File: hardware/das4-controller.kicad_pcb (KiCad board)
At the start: 4 copper layers, 51.1 x 94 mm, 78 parts, among them J1 USB-C, J2 USB-A 1, J3 USB-A 2, J4 Key matrix, Q1 2N7002, SW1 Button 1, SW2 Button 2, SW3 Button 3, SW4 Button 4, SW5 Button 5, SW6 BOOTSEL, SW7 RESET, U1 RP2350B, U2 CH334R, U3 W25Q128JVS, U4 ME6211C33M5G-N, Y1 12MHz, Y2 12MHz

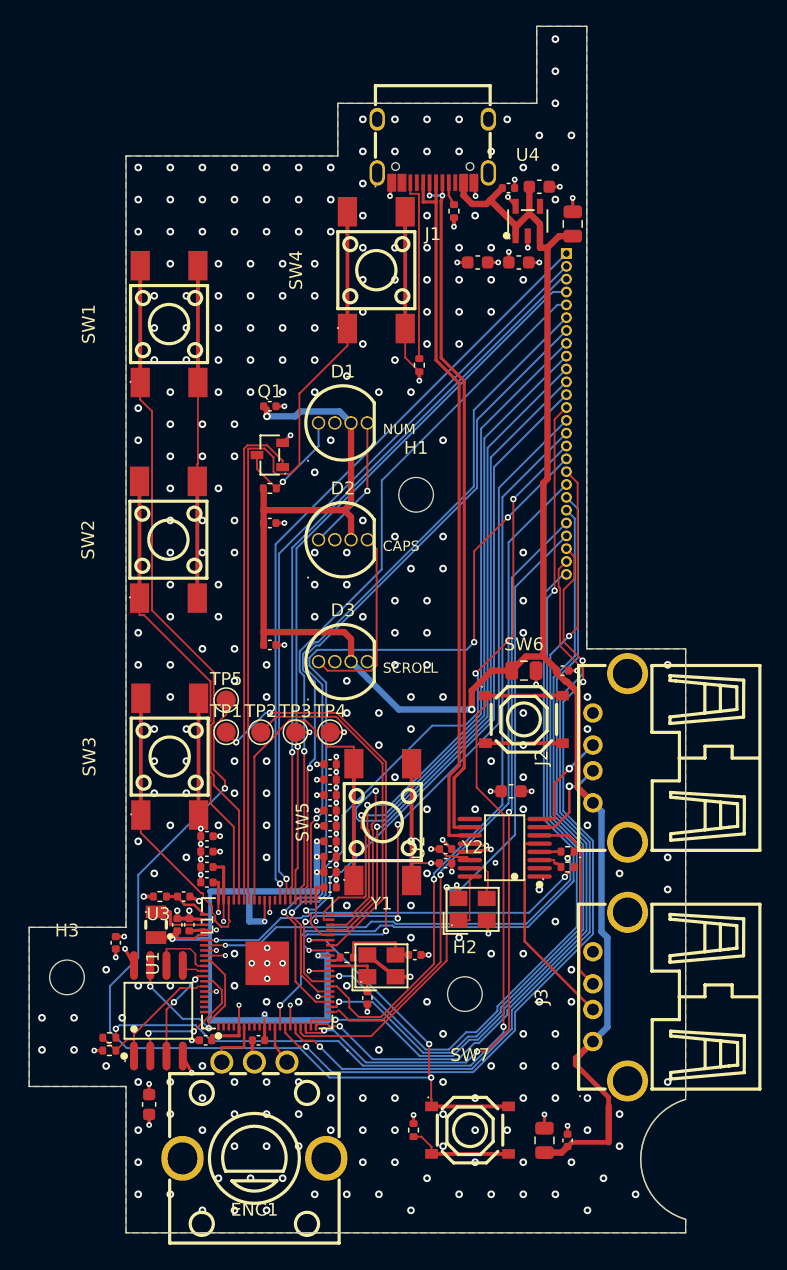
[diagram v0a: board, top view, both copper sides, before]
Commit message: J4: solder pads for the key PCB's 26-way 1.0 mm flex; re-route
The key PCB's flex cable ("CON2") is hot-bar soldered at both ends, so J4
is now 26 SMD pads (0.6 x 2.5 mm, 1.0 mm pitch) on the bottom side at the
board edge, hand-soldered like the original: no connector, no cost.
Keys only on the other end (no lights), so no 5 V check is needed.

Also:
- TP6/TP7 test pads for +1V1 and +5V (bring-up)
- router-only via band 0.5 mm round the USB_UP pair (layout review 2)
- a pre-placed via at each J4 pad so lines can arrive on either layer
- route.py cleanup: an unused via is removed and the track ends that met
  on it are linked inside its disc; zero-length tracks dropped
- route_best: 6 variants (Freerouting isn't fully deterministic here)

0 unconnected, 0 non-cosmetic DRC violations.

Co-Authored-By: Claude Opus 5.5 <noreply@anthropic.com>
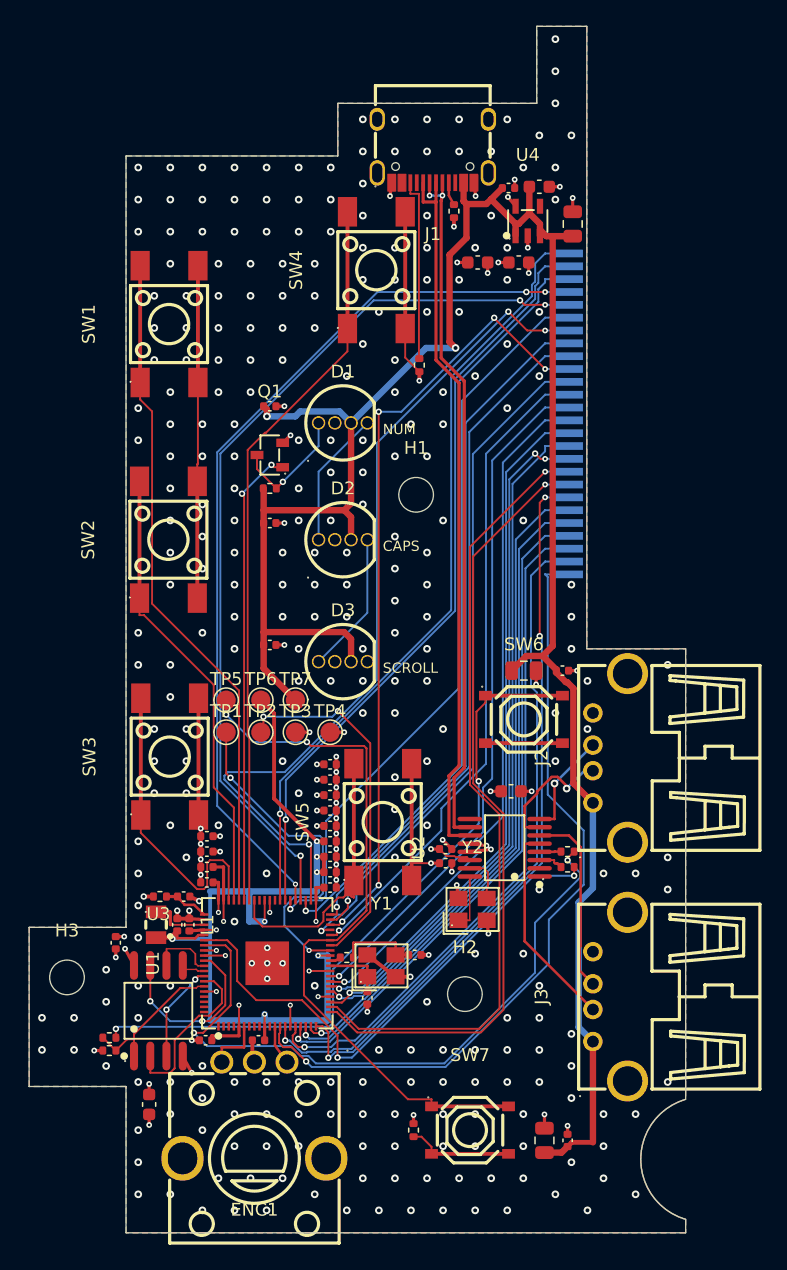
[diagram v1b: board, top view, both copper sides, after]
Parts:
- added TP6: TestPoint, TestPoint_Pad_D1.5mm, F.Cu at (110.5, 108.5)
- added TP7: TestPoint, TestPoint_Pad_D1.5mm, F.Cu at (113.2, 108.5)
- J4: value Key matrix -> Key matrix flex; footprint PinSocket_1x26_P1.00mm_Vertical -> FPC_Solder_1x26_P1.00mm
- moved J4 12.5 mm to (134.3, 86.2)
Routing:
- net RUN: track 82.1 -> 55.5 mm, vias 4 -> 2
- net N$6: track 33.3 -> 52.2 mm
- net KM13: track 67.8 -> 53.3 mm, vias 2 -> 1
- net KM5: track 55.7 -> 69.7 mm, vias 1 -> 3
- net KM4: track 56.8 -> 69.9 mm, vias 1 -> 3
- net +1V1: track 57.0 -> 69.8 mm
- net KM7: track 53.8 -> 66.5 mm, vias 1 -> 3
- net USB_BOOT: track 66.8 -> 54.3 mm
- net N$8: track 37.9 -> 26.4 mm, vias 4 -> 2
- net KM21: track 61.8 -> 51.3 mm
- net N$7: track 31.2 -> 41.6 mm
- net BTN5: track 31.6 -> 21.3 mm
- net KM24: track 62.7 -> 52.7 mm, vias 2 -> 1
- net KM25: track 62.7 -> 53.1 mm, vias 2 -> 1
- net KM17: track 62.4 -> 53.2 mm
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
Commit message: Check against RPi's "Hardware design with RP2350"; cap at DVDD pin 51
docs/rpi-guide-check-2026-09-26.md: section-by-section check of the
circuit and layout against the guide. Circuit matches RPi's reference
(regulator parts/values, flash, crystal, RUN/BOOTSEL/SWD, pinout).
- C151 moved right above DVDD pin 51 with its own GND via
- L1 orientation confirmed: JLC's library model has the polarity dot on
  pad 2 = +1V1, as in RPi's layout (Abracon datasheet + guide Fig. 4)
- docs/design.md: "Ordering at JLCPCB" (stackup, L1 dot check, hand parts)
- docs/bom.md regenerated (was stale); bom.csv lists both values when
  refs share a part (SW6 BOOTSEL / SW7 RESET)

0 unconnected, 0 non-cosmetic DRC violations.

Co-Authored-By: Claude Opus 5.5 <noreply@anthropic.com>
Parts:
- moved C151 5.18 mm to (110.8, 122.8), turned to 90 degrees
- moved C115 1.20 mm to (115.9, 114.7)
- moved C124 1.20 mm to (115.9, 118.3)
- moved C132 1.20 mm to (115.9, 121.9)
- moved C150 1.20 mm to (115.9, 119.5)
- moved C166 1.20 mm to (115.9, 120.7)
- moved C169 1.20 mm to (115.9, 115.9)
- moved C129 1.20 mm to (115.9, 117.1)
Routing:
- net KM22: track 51.5 -> 68.1 mm, vias 1 -> 3
- net KM5: track 69.7 -> 56.5 mm, vias 3 -> 1
- net KM4: track 69.9 -> 57.3 mm, vias 3 -> 1
- net KM26: track 60.8 -> 49.0 mm
- net KM18: track 61.5 -> 51.2 mm
- net N$8: track 26.4 -> 36.4 mm, vias 2 -> 4
- net KM19: track 60.8 -> 51.5 mm
- net USB_BOOT: track 54.3 -> 63.5 mm
- net KM10: track 61.4 -> 52.5 mm, vias 5 -> 1
- net N$6: track 52.2 -> 44.1 mm
- net KM25: track 53.1 -> 47.0 mm, vias 1 -> 3
- net KM24: track 52.7 -> 47.4 mm, vias 1 -> 3
- net QSPI_SD1: track 13.1 -> 8.06 mm, vias 0 -> 2
- net BTN5: track 21.3 -> 25.9 mm, vias 0 -> 2
- net KM23: track 51.7 -> 56.1 mm, vias 1 -> 3
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
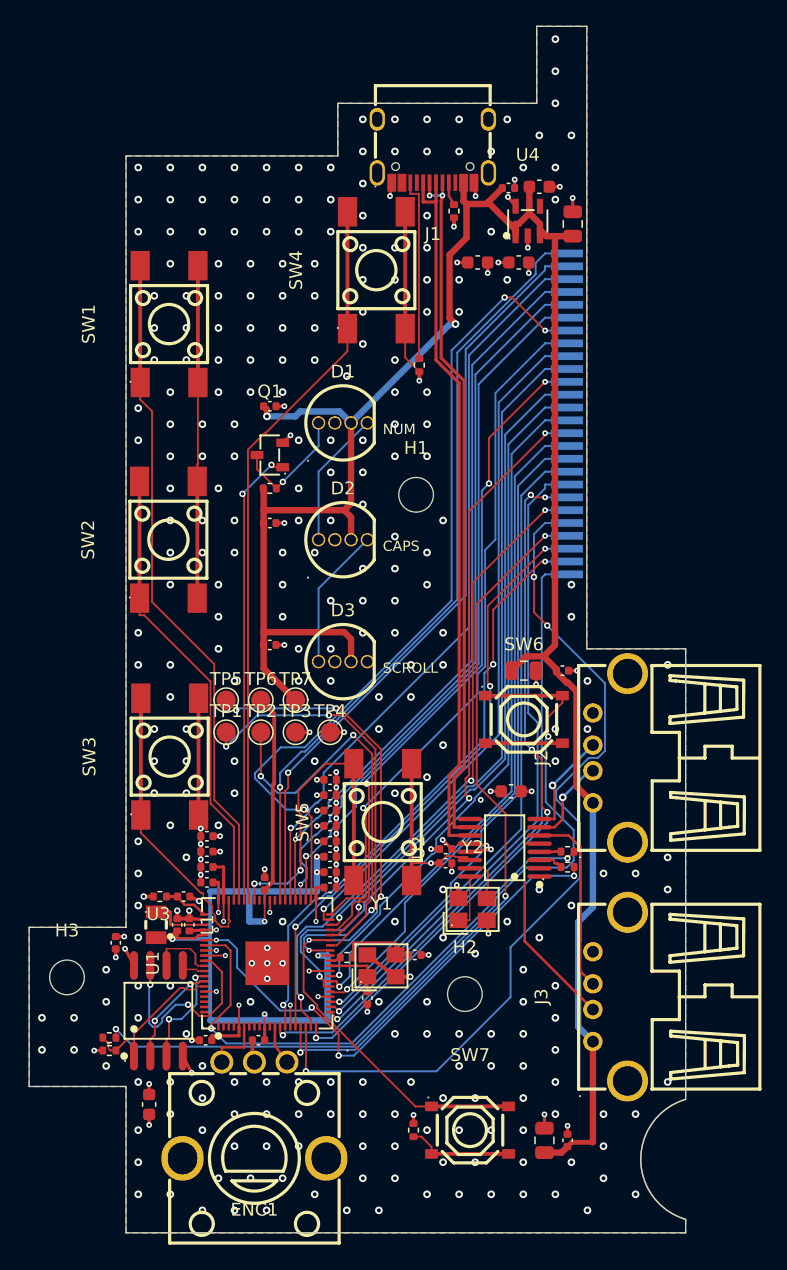
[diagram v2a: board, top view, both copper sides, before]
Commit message: UART0 debug pads, silkscreen tidy, re-route
- TP8/TP9/TP10 on the left tab: UART0 TX (GPIO0), RX (GPIO1), GND, a
  serial console for bring-up (firmware check suggestion)
- silkscreen: references only on SW1-SW5 and J4; the rest on F.Fab so
  nothing prints over neighbouring parts. Test pads get function labels
  (SWC, SWD, GND, 3V3, RUN, 1V1, 5V, TX, RX), SW6/SW7 read BOOT/RST
- route.py: trim_dangling() removes signal-track dead ends after the via
  cleanup (this board: a 2-segment KM24 stub, trimmed after routing)

0 unconnected, 0 non-cosmetic DRC violations.

Co-Authored-By: Claude Opus 5.5 <noreply@anthropic.com>
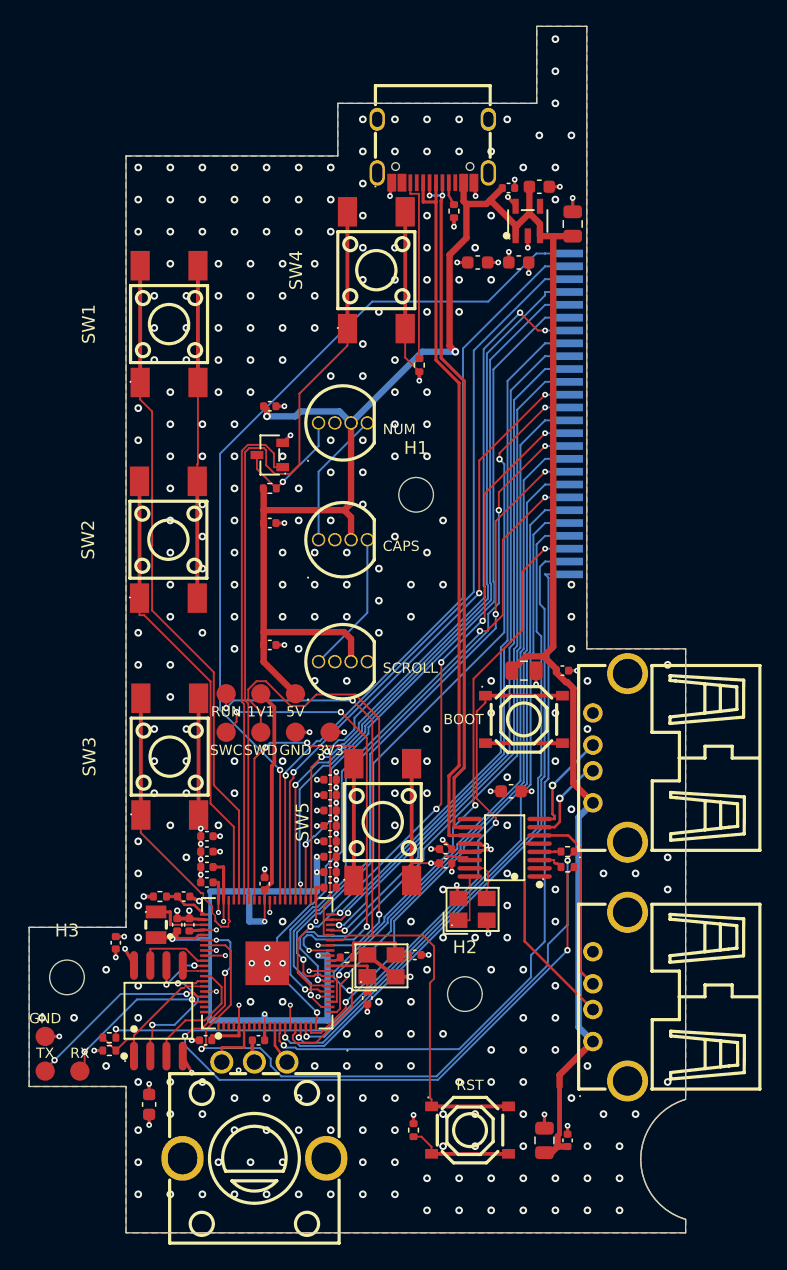
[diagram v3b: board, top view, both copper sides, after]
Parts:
- added TP10: TestPoint, TestPoint_Pad_D1.5mm, F.Cu at (93.7, 134.7)
- added TP8: TestPoint, TestPoint_Pad_D1.5mm, F.Cu at (93.7, 137.4)
- added TP9: TestPoint, TestPoint_Pad_D1.5mm, F.Cu at (96.4, 137.4)
- moved TP5 0.50 mm to (107.8, 108.0)
- moved TP6 0.50 mm to (110.5, 108.0)
- moved TP7 0.50 mm to (113.2, 108.0)
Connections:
- U1 pad 77: (no net) -> N$10
- U1 pad 78: (no net) -> N$11
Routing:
- net KM22: track 68.1 -> 51.1 mm, vias 3 -> 1
- net N$10: track 0.00 -> 15.1 mm, vias 0 -> 2
- net N$7: track 41.0 -> 53.8 mm
- net N$11: track 0.00 -> 12.7 mm, vias 0 -> 2
- net QSPI_SD3: track 16.2 -> 5.89 mm, vias 2 -> 0
- net KM1: track 60.8 -> 70.2 mm
- net N$6: track 44.1 -> 52.4 mm
- net KM26: track 49.0 -> 57.1 mm
- net USB_BOOT: track 63.5 -> 55.5 mm
- net KM7: track 64.7 -> 57.3 mm
- net N$9: track 31.7 -> 38.5 mm
- net BTN4: track 56.9 -> 62.5 mm
- net KM24: track 47.4 -> 52.0 mm
- net KM23: track 56.1 -> 51.6 mm, vias 3 -> 1
- net KM25: track 47.0 -> 51.0 mm, vias 3 -> 1
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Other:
- board text added: "1V1"
- board text added: "3V3"
- board text added: "5V"
- board text added: "BOOT"
- board text added: "GND"
- board text added: "RST"
- board text added: "RUN"
- board text added: "RX"
- board text added: "SWC"
- board text added: "SWD"
- board text added: "TX"
